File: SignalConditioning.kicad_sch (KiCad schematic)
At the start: 51 parts, among them J10 Screw_Terminal_01x02, J9 Screw_Terminal_01x04

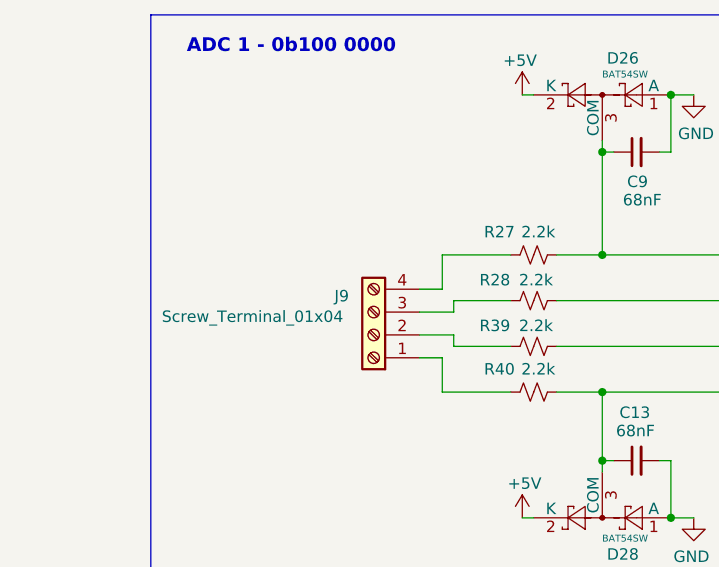
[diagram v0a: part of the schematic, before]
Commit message: Add current sensing and fuse mount for IGN
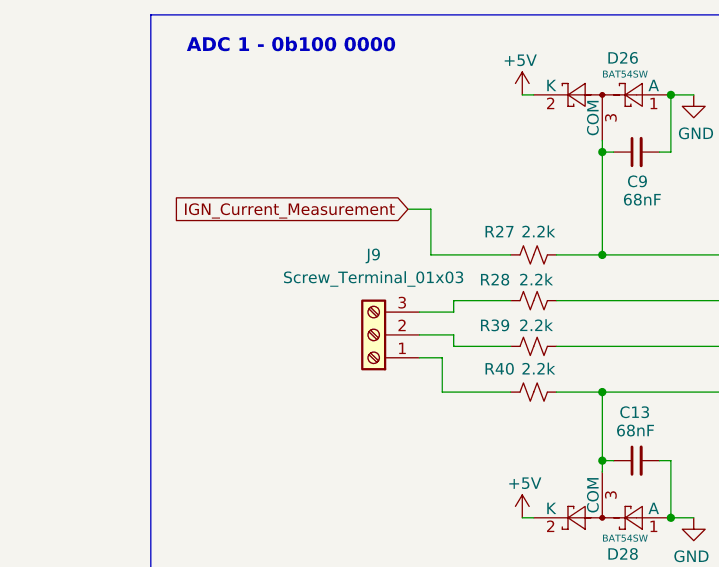
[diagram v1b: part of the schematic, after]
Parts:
- removed J9: Screw_Terminal_01x04, TerminalBlock:TerminalBlock_Xinya_XY308-2.54-4P_1x04_P2.54mm_Horizontal, symbol Connector:Screw_Terminal_01x04
- added J9: Screw_Terminal_01x03, TerminalBlock:TerminalBlock_Xinya_XY308-2.54-3P_1x03_P2.54mm_Horizontal, symbol Connector:Screw_Terminal_01x03
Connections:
- net IGN_Current_Measurement: now reaches R27.1
- net at R39.1: now also J9.2 (Pin_2)
- net at R28.1: now also J9.3 (Pin_3)
- net at R40.1: now also J9.1 (Pin_1)
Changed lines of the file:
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@@
 	(wire
 		(pts
-			(xy 62.23 48.26) (xy 62.23 44.45)
+			(xy 60.96 39.37) (xy 60.96 44.45)
 		)
 		(stroke
@@
 	(wire
 		(pts
-			(xy 62.23 44.45) (xy 69.85 44.45)
+			(xy 60.96 44.45) (xy 69.85 44.45)
 		)
 		(stroke
@@
 	(wire
 		(pts
-			(xy 59.69 48.26) (xy 62.23 48.26)
+			(xy 58.42 39.37) (xy 60.96 39.37)
 		)
 		(stroke
@@
 		)
 	)
+	(global_label "IGN_Current_Measurement"
+		(shape input)
+		(at 58.42 39.37 180)
+		(fields_autoplaced yes)
+		(effects
+			(font
+				(size 1.27 1.27)
+			)
+			(justify right)
+		)
+		(property "Intersheetrefs" "${INTERSHEET_REFS}"
+			(at 30.9421 39.37 0)
+			(effects
+				(font
+					(size 1.27 1.27)
+				)
+				(justify right)
+				(hide yes)
+			)
+		)
+	)
 	(global_label "PT_READING_6"
 		(shape input)
@@
 	)
 	(symbol
-		(lib_id "Connector:Screw_Terminal_01x04")
-		(at 54.61 53.34 180)
-		(unit 1)
-		(exclude_from_sim no)
-		(in_bom no)
-		(on_board yes)
-		(dnp no)
-		(property "Reference" "J9"
-			(at 51.054 49.022 0)
-			(effects
-				(font
-					(size 1.27 1.27)
-				)
-			)
-		)
-		(property "Value" "Screw_Terminal_01x04"
-			(at 41.148 51.308 0)
-			(effects
-				(font
-					(size 1.27 1.27)
-				)
-			)
-		)
-		(property "Footprint" "TerminalBlock:TerminalBlock_Xinya_XY308-2.54-4P_1x04_P2.54mm_Horizontal"
-			(at 54.61 53.34 0)
-			(effects
-				(font
-					(size 1.27 1.27)
-				)
-				(hide yes)
-			)
-		)
-		(property "Datasheet" "~"
-			(at 54.61 53.34 0)
-			(effects
-				(font
-					(size 1.27 1.27)
-				)
-				(hide yes)
-			)
-		)
-		(property "Description" "Generic screw terminal, single row, 01x04, script generated (kicad-library-utils/schlib/autogen/connector/)"
-			(at 54.61 53.34 0)
-			(effects
-				(font
-					(size 1.27 1.27)
-				)
-				(hide yes)
-			)
-		)
-		(property "Digikey PN" "ED10563-ND"
-			(at 54.61 53.34 0)
-			(effects
-				(font
-					(size 1.27 1.27)
-				)
-				(hide yes)
-			)
-		)
-		(pin "2"
-		)
-		(pin "4"
-		)
-		(pin "1"
-		)
-		(pin "3"
-		)
-		(instances
-			(project "panda"
-				(path "/226c5870-4123-4efa-a2b3-b42d02f59bb7/21243b6d-fc9e-4696-b2f4-96a9d8b17f22/f1423c59-a220-4b9a-be1b-1c4e29a8b304"
-					(reference "J9")
-					(unit 1)
-				)
-			)
-		)
-	)
-	(symbol
 		(lib_id "Device:C_Small")
 		(at 111.76 146.05 90)
@@
 					(unit 1)
 				)
+			)
+		)
+	)
+	(symbol
+		(lib_id "Connector:Screw_Terminal_01x03")
+		(at 54.61 53.34 180)
+		(unit 1)
+		(exclude_from_sim no)
+		(in_bom yes)
+		(on_board yes)
+		(dnp no)
+		(fields_autoplaced yes)
+		(property "Reference" "J9"
+			(at 54.61 44.45 0)
+			(effects
+				(font
+					(size 1.27 1.27)
+				)
+			)
+		)
+		(property "Value" "Screw_Terminal_01x03"
+			(at 54.61 46.99 0)
+			(effects
+				(font
+					(size 1.27 1.27)
+				)
+			)
+		)
+		(property "Footprint" "TerminalBlock:TerminalBlock_Xinya_XY308-2.54-3P_1x03_P2.54mm_Horizontal"
+			(at 54.61 53.34 0)
+			(effects
+				(font
+					(size 1.27 1.27)
+				)
+				(hide yes)
+			)
+		)
+		(property "Datasheet" "~"
+			(at 54.61 53.34 0)
+			(effects
+				(font
+					(size 1.27 1.27)
+				)
+				(hide yes)
+			)
+		)
+		(property "Description" "Generic screw terminal, single row, 01x03, script generated (kicad-library-utils/schlib/autogen/connector/)"
+			(at 54.61 53.34 0)
+			(effects
+				(font
+					(size 1.27 1.27)
+				)
+				(hide yes)
+			)
+		)
+		(pin "3"
+		)
+		(pin "1"
+		)
+		(pin "2"
+		)
+		(instances
+			(project ""
+				(path "/226c5870-4123-4efa-a2b3-b42d02f59bb7/21243b6d-fc9e-4696-b2f4-96a9d8b17f22/f1423c59-a220-4b9a-be1b-1c4e29a8b304"
+					(reference "J9")
+					(unit 1)
+				)

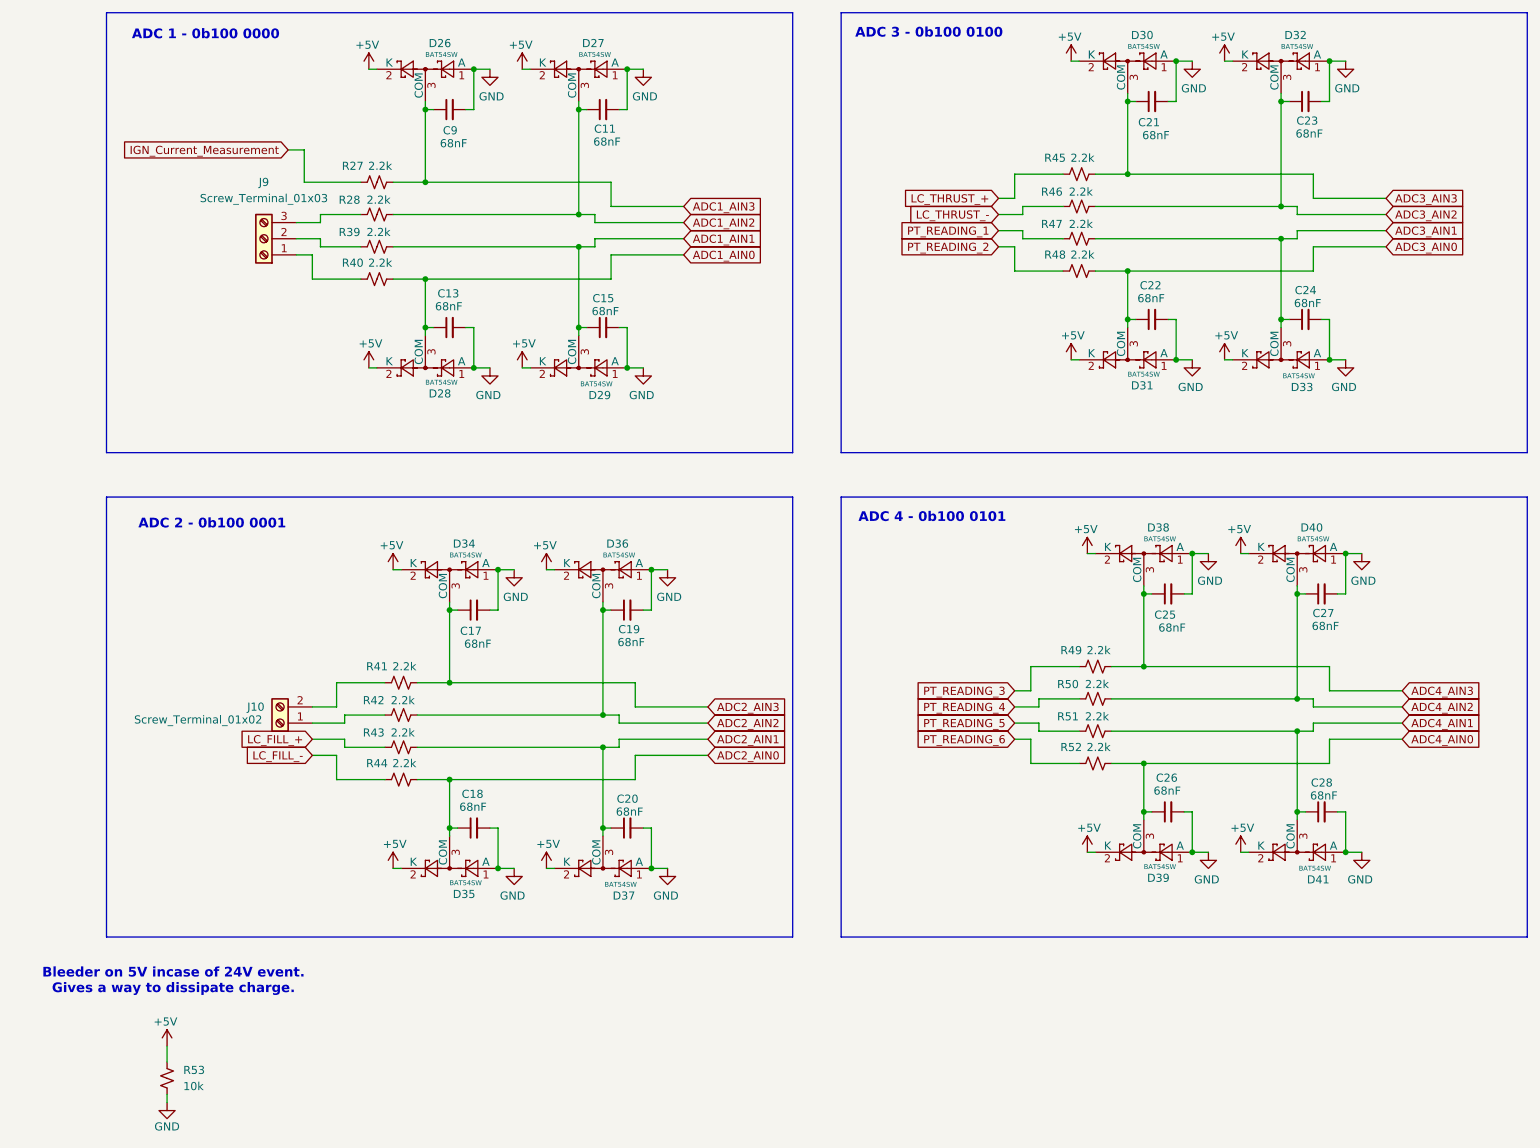
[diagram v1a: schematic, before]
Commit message: connected to GPIO pins
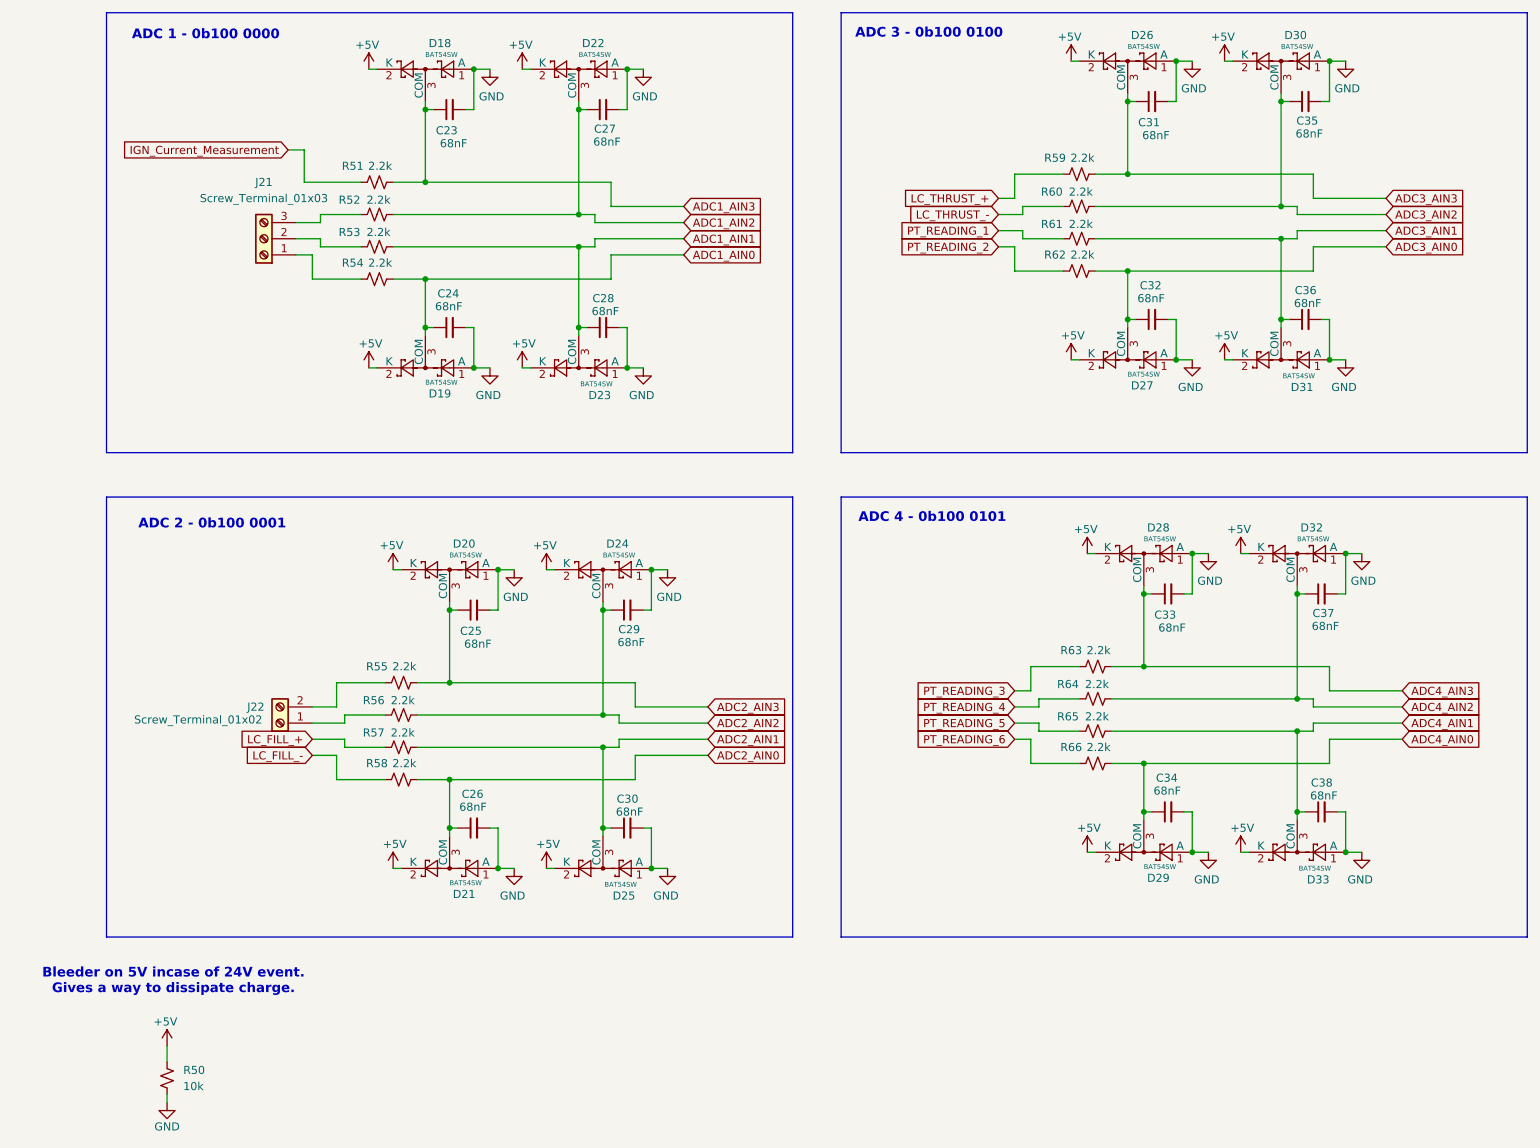
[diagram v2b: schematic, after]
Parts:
- renumbered C9 to C23, C13 to C24, C17 to C25, C18 to C26, C11 to C27, C15 to C28, C19 to C29, C20 to C30, C21 to C31, C22 to C32, C25 to C33, C26 to C34, C23 to C35, C24 to C36, C27 to C37, C28 to C38, D26 to D18, D28 to D19, D34 to D20, D35 to D21, D27 to D22, D29 to D23, D36 to D24, D37 to D25, D30 to D26, D31 to D27, D38 to D28, D39 to D29, D32 to D30, D33 to D31, D40 to D32, D41 to D33, J9 to J21, J10 to J22, R53 to R50, R27 to R51, R28 to R52, R39 to R53, R40 to R54, R41 to R55, R42 to R56, R43 to R57, R44 to R58, R45 to R59, R46 to R60, R47 to R61, R48 to R62, R49 to R63, R50 to R64, R51 to R65, R52 to R66

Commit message: added 24V lockout key LED indicator
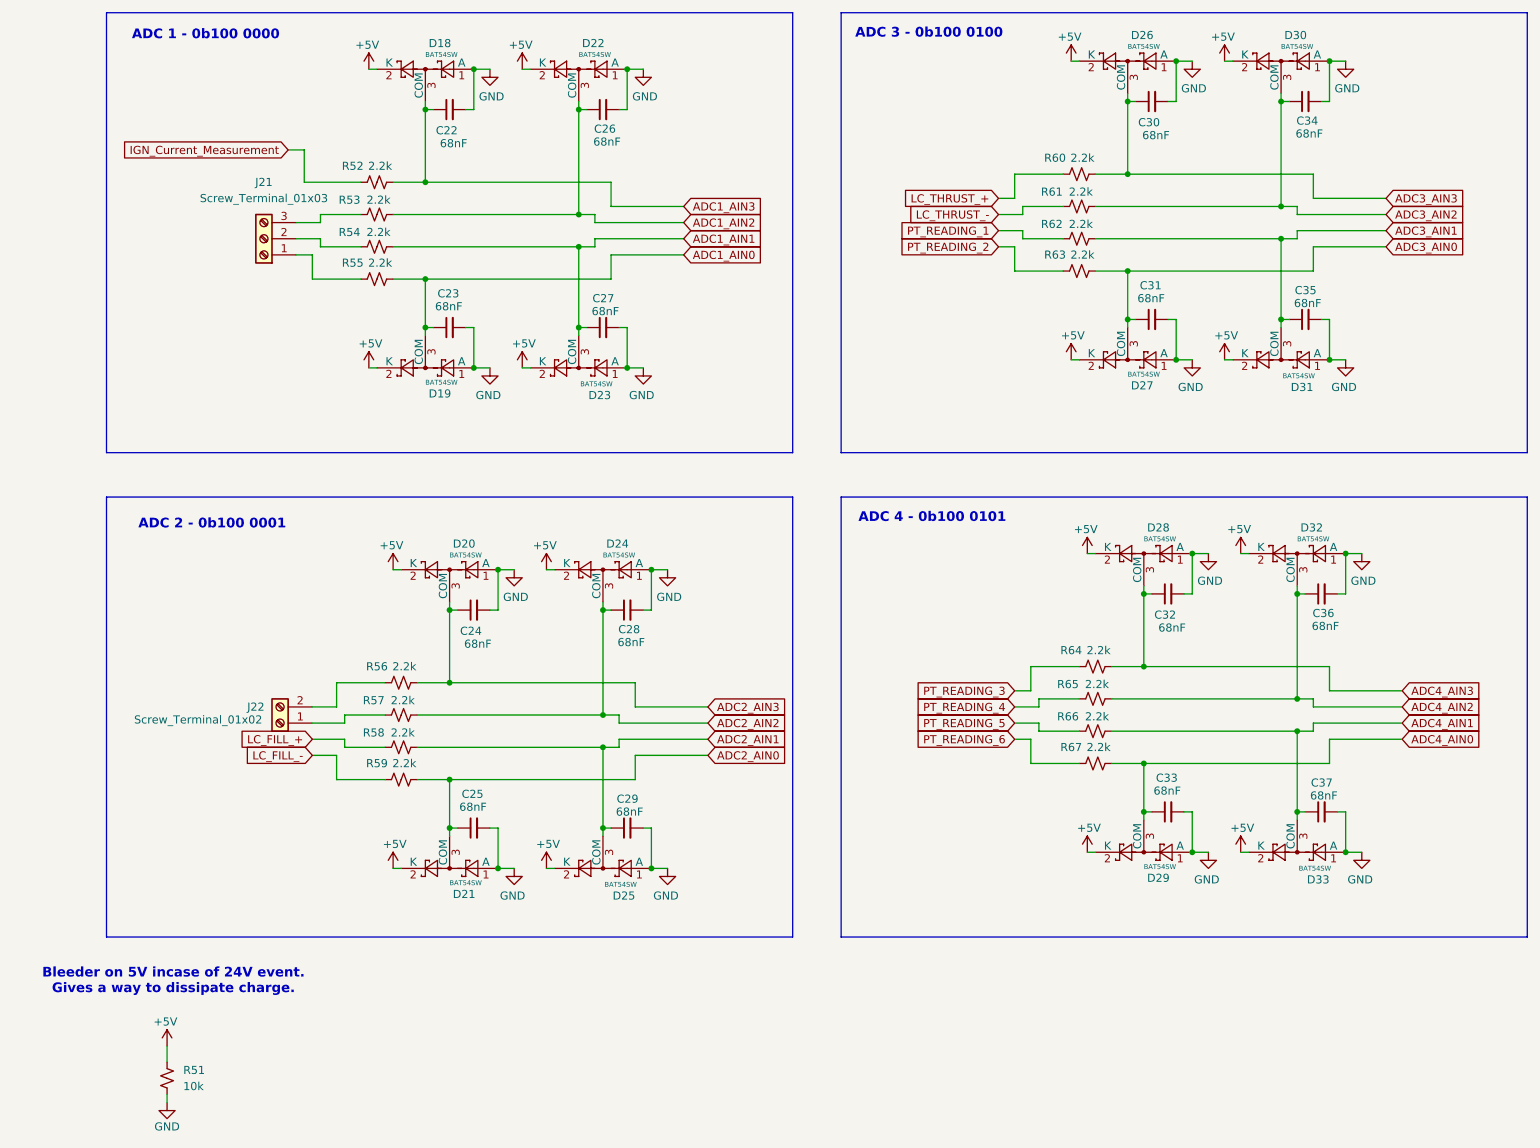
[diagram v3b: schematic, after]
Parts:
- renumbered C23 to C22, C24 to C23, C25 to C24, C26 to C25, C27 to C26, C28 to C27, C29 to C28, C30 to C29, C31 to C30, C32 to C31, C33 to C32, C34 to C33, C35 to C34, C36 to C35, C37 to C36, C38 to C37, R50 to R51, R51 to R52, R52 to R53, R53 to R54, R54 to R55, R55 to R56, R56 to R57, R57 to R58, R58 to R59, R59 to R60, R60 to R61, R61 to R62, R62 to R63, R63 to R64, R64 to R65, R65 to R66, R66 to R67

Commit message: pcb first draft, changed esp32 pin connections
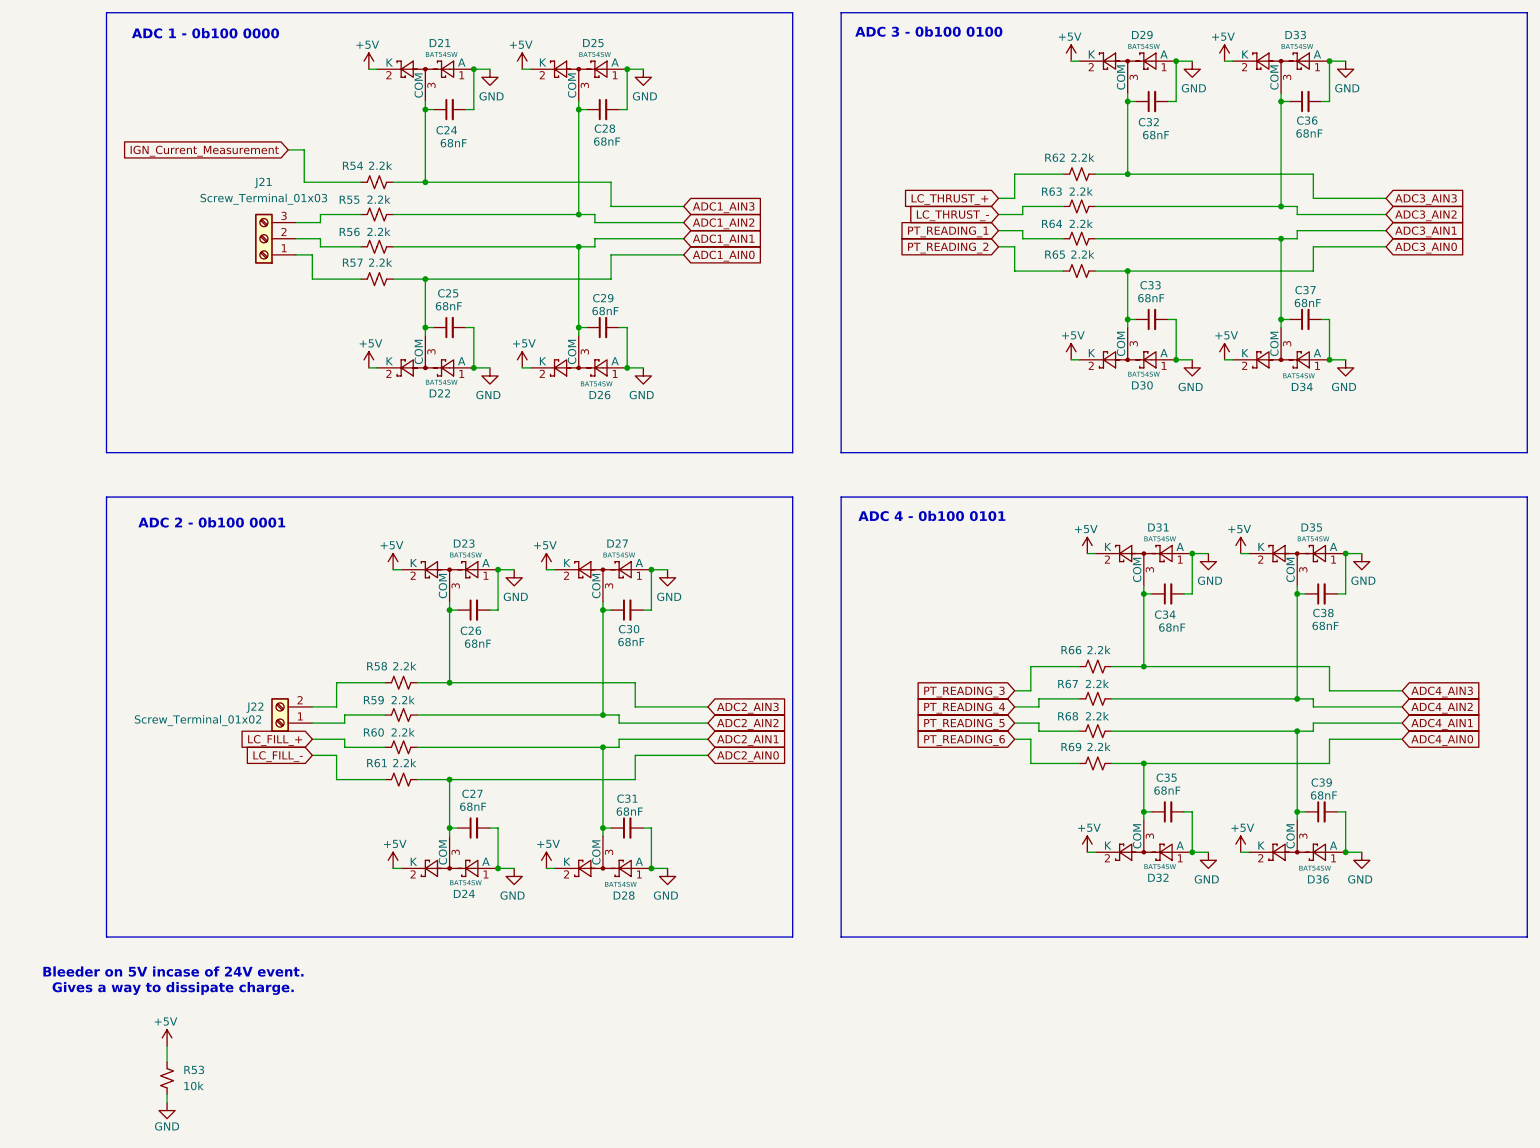
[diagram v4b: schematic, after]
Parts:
- renumbered C22 to C24, C23 to C25, C24 to C26, C25 to C27, C26 to C28, C27 to C29, C28 to C30, C29 to C31, C30 to C32, C31 to C33, C32 to C34, C33 to C35, C34 to C36, C35 to C37, C36 to C38, C37 to C39, D18 to D21, D19 to D22, D20 to D23, D21 to D24, D22 to D25, D23 to D26, D24 to D27, D25 to D28, D26 to D29, D27 to D30, D28 to D31, D29 to D32, D30 to D33, D31 to D34, D32 to D35, D33 to D36, R51 to R53, R52 to R54, R53 to R55, R54 to R56, R55 to R57, R56 to R58, R57 to R59, R58 to R60, R59 to R61, R60 to R62, R61 to R63, R62 to R64, R63 to R65, R64 to R66, R65 to R67, R66 to R68, R67 to R69
